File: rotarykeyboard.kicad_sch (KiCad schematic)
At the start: 21 parts, among them J101 Breakout, J102 Cortex Debug, SW101 RotaryEncoder, SW102 KBPush, SW103 RESET, U101 ATSAMDA1E14B-ABT

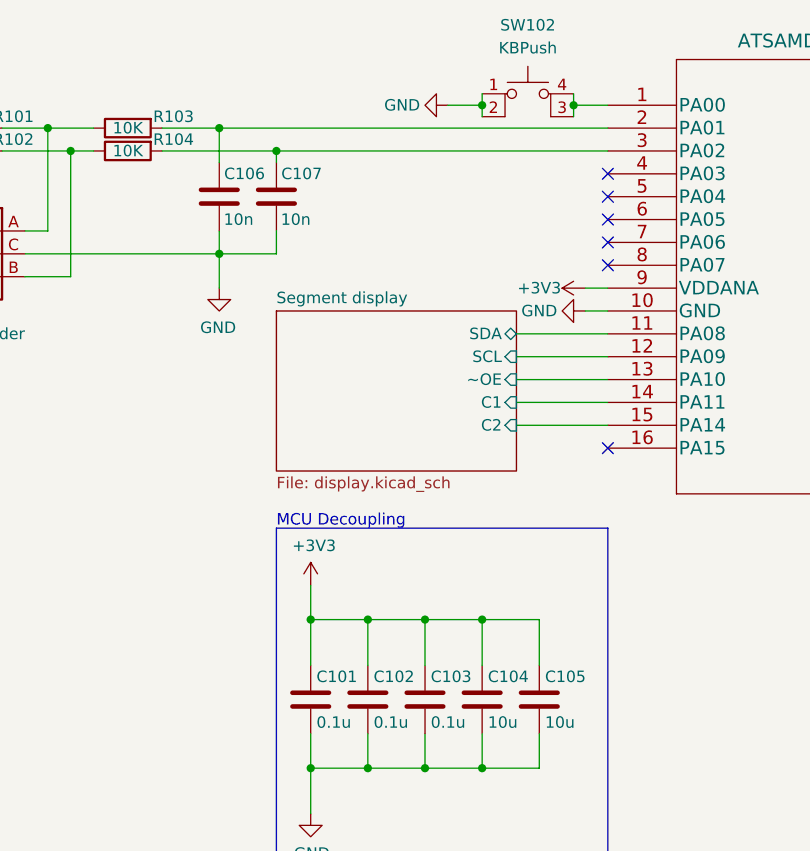
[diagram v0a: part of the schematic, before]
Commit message: replace out of stock components
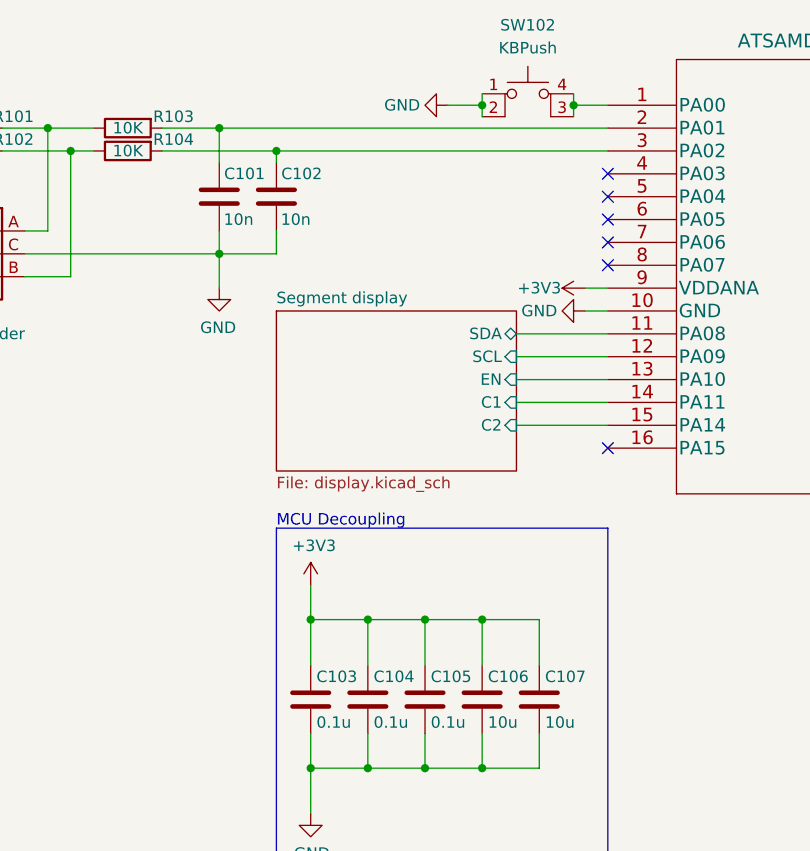
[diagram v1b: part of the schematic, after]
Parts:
- renumbered C106 to C101, C107 to C102, C101 to C103, C102 to C104, C103 to C105, C104 to C106, C105 to C107
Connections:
- net Segment display/~OE renamed Segment display/EN
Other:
- sheet Segment display ports: added EN; removed ~OE

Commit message: final component changes
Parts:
- C101, C102: value 10n -> (none); footprint Capacitor_SMD:C_0805_2012Metric -> (none)
- C103, C104, C105, C108: value 0.1u -> (none); footprint Capacitor_SMD:C_0805_2012Metric -> (none)
- C106, C107: value 10u -> (none); footprint Capacitor_SMD:C_0805_2012Metric -> (none)
- C109: value 1u -> (none); footprint Capacitor_SMD:C_0805_2012Metric -> (none)
- J101: value Breakout -> (none); footprint Connector_PinHeader_1.27mm:PinHeader_2x04_P1.27mm_Vertical -> (none)
- J102: value Cortex Debug -> (none); footprint Connector_PinHeader_1.27mm:PinHeader_2x05_P1.27mm_Vertical -> (none)
- R101, R102, R103, R104: value 10K -> (none); footprint Resistor_SMD:R_0805_2012Metric -> (none)
- R105: value 330 -> (none); footprint Resistor_SMD:R_0805_2012Metric -> (none)
- R106: value 1k -> (none); footprint Resistor_SMD:R_0805_2012Metric -> (none)
- SW101: value RotaryEncoder -> (none); footprint EVQV6:EVQV6 -> (none)
- SW102: value KBPush -> (none); footprint TL3305A:SW_SPST_TL3305A -> (none)
- SW103: value RESET -> (none); footprint TL3305A:SW_SPST_TL3305A -> (none)
- U101: value ATSAMDA1E14B-ABT -> (none); footprint Package_QFP:TQFP-32_7x7mm_P0.8mm -> (none)
